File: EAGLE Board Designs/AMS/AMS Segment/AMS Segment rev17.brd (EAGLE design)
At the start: 275.2 x 86 mm, 338 parts, among them J1 CONNECTOR-2_MICROFIT_SMD_RIGH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, J10 CONNECTOR-2_MICROFIT_SMD_RIGH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, J100 CONNECTOR-1_5222_, J101 CONNECTOR-1_5222_, J102 CONNECTOR-1_5222_, J103 CONNECTOR-1_5222_, J104 CONNECTOR-1_5222_, J105 CONNECTOR-1_5222_, J106 CONNECTOR-1_5222_, J107 CONNECTOR-1_5222_, J108 CONNECTOR-1_5222_, J109 CONNECTOR-1_5222_, J110 CONNECTOR-1_5222_, J111 CONNECTOR-1_5222_, J112 CONNECTOR-1_5222_, J113 CONNECTOR-1_5222_, J114 CONNECTOR-1_5222_, J115 CONNECTOR-1_5222_, J116 CONNECTOR-1_5222_, J117 CONNECTOR-1_5222_, J118 CONNECTOR-1_5222_, J119 CONNECTOR-1_5222_, J120 CONNECTOR-1_5222_, J121 CONNECTOR-1_5222_, J2 CONNECTOR-2_MICROFIT_SMD_RIGH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, J3 CONNECTOR-2_MICROFIT_SMD_RIGH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, J4 CONNECTOR-2_MICROFIT_SMD_RIGH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, J5 CONNECTOR-2_MICROFIT_SMD_RIGH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, J6 CONNECTOR-2_MICROFIT_SMD_RIGH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, J7 CONNECTOR-2_MICROFIT_SMD_RIGH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, J8 CONNECTOR-2_MICROFIT_SMD_RIGH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, J9 CONNECTOR-2_MICROFIT_SMD_RIGH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, T1 TRANSFORMER_HM2112ZNLT, U1 LTC6811-2, U2 LTC6811-2, U3 SHT31-ARP-B, U4 SHT31-ARP-B, U5 LT3990-5, U6 LT3990-5

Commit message: Renamed to rev17
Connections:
- net GPIO4L: now also R47.2; no longer R47.1
- net N$90: now also R47.1; no longer R47.2
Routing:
- net VREGL: track 269.5 -> 256.8 mm
- net GPIO4L: track 78.6 -> 74.3 mm
- net N$90: track 23.1 -> 24.3 mm
- net V-L: track 134.3 -> 133.6 mm

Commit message: Working on board changes
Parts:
- moved R48 3.73 mm to (73.2, -3.61)
- moved C29 3.73 mm to (73.2, -6.52)
- moved R45 3.73 mm to (73.2, -9.42)
- moved C31 2.18 mm to (212.2, -8.03)
- moved R46 2.18 mm to (212.2, -10.9)
- moved R50 2.18 mm to (212.2, -5.11)
- moved R10 0.33 mm to (107.3, -71.3)
- moved R11 0.33 mm to (110.8, -71.3)
- moved R8 0.33 mm to (100.4, -71.3)
- moved R9 0.33 mm to (103.9, -71.3)
- turned C30 to 270 degrees
- turned R44 to 270 degrees
- turned R49 to 270 degrees
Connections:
- net CELL10:N$5 renamed CELL10:QG
- net CELL10:N$6 renamed CELL10:QD
- net CELL10:N$7 renamed CELL10:LED
- net CELL11:N$5 renamed CELL11:QG
- net CELL11:N$6 renamed CELL11:QD
- net CELL11:N$7 renamed CELL11:LED
- net CELL12:N$5 renamed CELL12:QG
- net CELL12:N$6 renamed CELL12:QD
- net CELL12:N$7 renamed CELL12:LED
- net CELL13:N$5 renamed CELL13:QG
- net CELL13:N$6 renamed CELL13:QD
- net CELL13:N$7 renamed CELL13:LED
- net CELL14:N$5 renamed CELL14:QG
- net CELL14:N$6 renamed CELL14:QD
- net CELL14:N$7 renamed CELL14:LED
- net CELL15:N$5 renamed CELL15:QG
- net CELL15:N$6 renamed CELL15:QD
- net CELL15:N$7 renamed CELL15:LED
- net CELL16:N$5 renamed CELL16:QG
- net CELL16:N$6 renamed CELL16:QD
- net CELL16:N$7 renamed CELL16:LED
- net CELL17:N$5 renamed CELL17:QG
- net CELL17:N$6 renamed CELL17:QD
- net CELL17:N$7 renamed CELL17:LED
- net CELL18:N$5 renamed CELL18:QG
- net CELL18:N$6 renamed CELL18:QD
- net CELL18:N$7 renamed CELL18:LED
- net CELL19:N$5 renamed CELL19:QG
- net CELL19:N$6 renamed CELL19:QD
- net CELL19:N$7 renamed CELL19:LED
- net CELL1:N$5 renamed CELL1:QG
- net CELL1:N$6 renamed CELL1:QD
- net CELL1:N$7 renamed CELL1:LED
- net CELL20:N$5 renamed CELL20:QG
- net CELL20:N$6 renamed CELL20:QD
- net CELL20:N$7 renamed CELL20:LED
- net CELL21:N$5 renamed CELL21:QG
- net CELL21:N$6 renamed CELL21:QD
- net CELL21:N$7 renamed CELL21:LED
- net CELL2:N$5 renamed CELL2:QG
- net CELL2:N$6 renamed CELL2:QD
- net CELL2:N$7 renamed CELL2:LED
- net CELL3:N$5 renamed CELL3:QG
- net CELL3:N$6 renamed CELL3:QD
- net CELL3:N$7 renamed CELL3:LED
- net CELL4:N$5 renamed CELL4:QG
- net CELL4:N$6 renamed CELL4:QD
- net CELL4:N$7 renamed CELL4:LED
- net CELL5:N$5 renamed CELL5:QG
- net CELL5:N$6 renamed CELL5:QD
- net CELL5:N$7 renamed CELL5:LED
- net CELL6:N$5 renamed CELL6:QG
- net CELL6:N$6 renamed CELL6:QD
- net CELL6:N$7 renamed CELL6:LED
- net CELL7:N$5 renamed CELL7:QG
- net CELL7:N$6 renamed CELL7:QD
- net CELL7:N$7 renamed CELL7:LED
- net CELL8:N$5 renamed CELL8:QG
- net CELL8:N$6 renamed CELL8:QD
- net CELL8:N$7 renamed CELL8:LED
- net CELL9:N$5 renamed CELL9:QG
- net CELL9:N$6 renamed CELL9:QD
- net CELL9:N$7 renamed CELL9:LED
- net GPIO1U: now also C30.2, R44.1; no longer C30.1, R44.2
- net N$71: now also R44.2; no longer R44.1
- net V-U: now also C30.1; no longer C30.2
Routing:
- net N$67: track 61.1 -> 40.1 mm
- net VREGL: track 256.8 -> 245.3 mm
- net V-L: track 133.6 -> 124.4 mm, vias 36 -> 35
- net N$68: track 42.9 -> 35.1 mm
- net S7U: track 79.2 -> 72.0 mm
- net C7U: track 77.3 -> 71.0 mm
- net V-U: track 166.2 -> 162.5 mm
- net GPIO2U: track 82.6 -> 85.6 mm
- net N$76: track 21.1 -> 24.2 mm
- net N$90: track 24.3 -> 21.5 mm
- net N$71: track 19.4 -> 21.1 mm
- net C6U: track 51.7 -> 50.5 mm
- net GPIO3L: track 55.6 -> 56.6 mm
- net N$88: track 21.1 -> 22.1 mm
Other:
- board text added: "HyTech Racing 2022 AMS Segment rev17 Designed by Cody Kaminsky, Noah Bruckner, and Ethan Weinstock Based on rev15 by Arvind Srinivasan"
- board text removed: "HyTech Racing 2022 AMS Segment rev17 Designed by Cody Kaminsky and Noah Bruckner based on rev15 by Arvind Srinivasan"

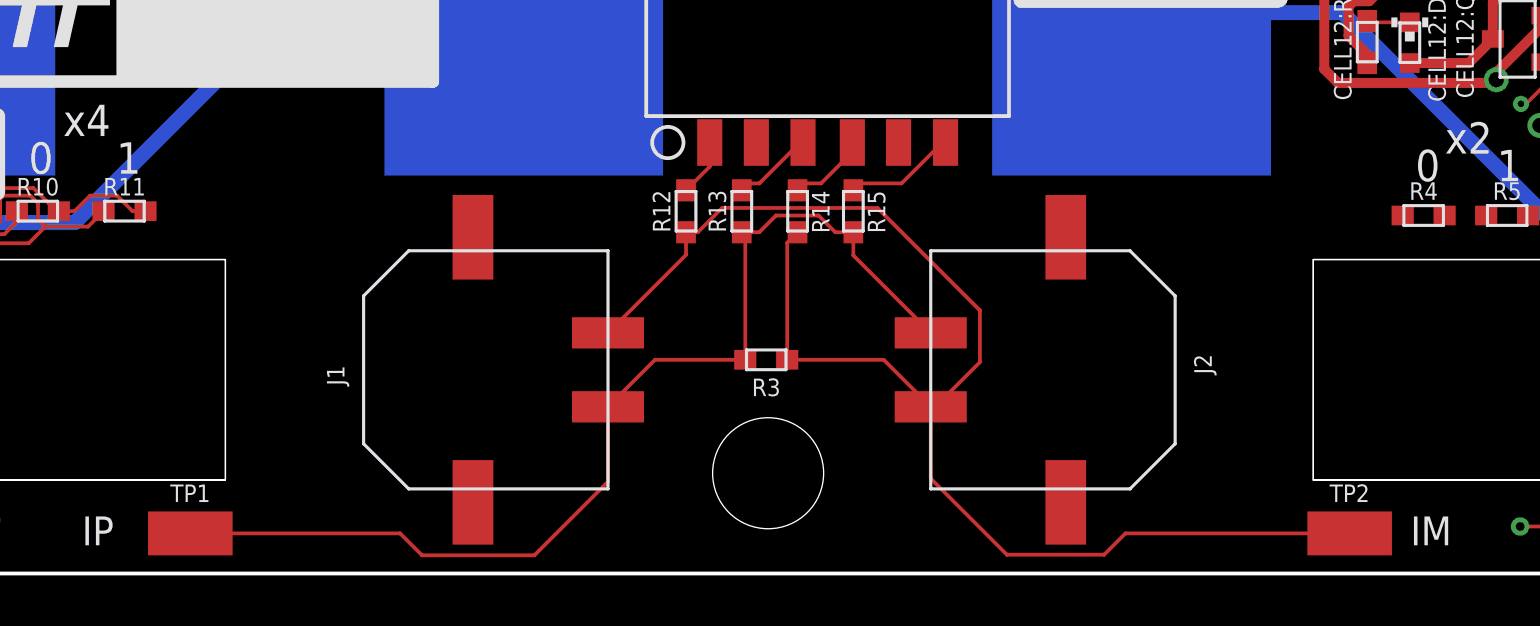
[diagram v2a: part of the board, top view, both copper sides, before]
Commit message: Update AMS Segment rev17.brd
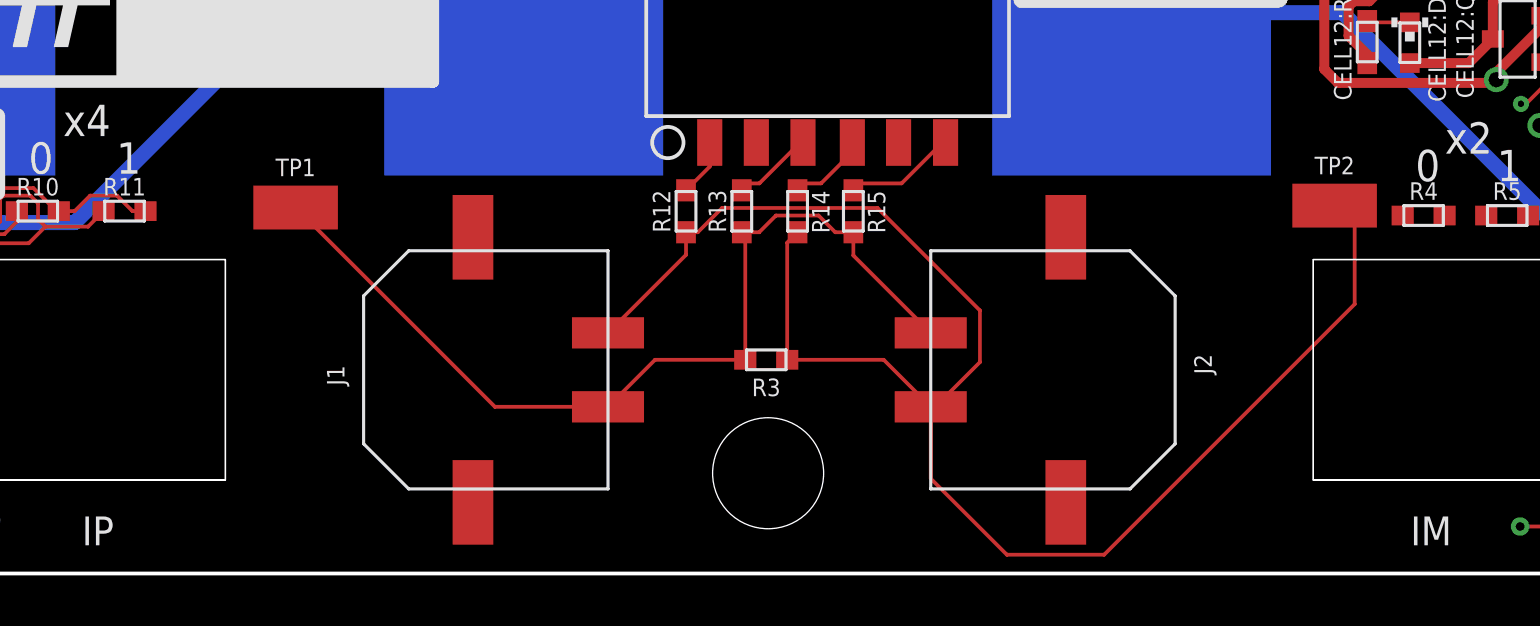
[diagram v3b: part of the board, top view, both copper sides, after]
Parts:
- moved TP1 13.9 mm to (117.8, -71.1)
- moved TP2 13.3 mm to (159.9, -71.1)
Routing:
- net IM: track 57.7 -> 66.4 mm
- net IP: track 43.6 -> 38.0 mm
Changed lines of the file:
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@@
 <attribute name="NAME" x="89.1286" y="-20.0533" size="0.7112" layer="25" font="vector" rot="R270" align="bottom-center"/>
 </element>
-<element name="TP1" library="HyTechDevices" package="MICRO_MINIATURE" value="TEST_POINT" x="113.4872" y="-84.3534" smashed="yes">
-<attribute name="DKPN" value="36-5015CT-ND" x="113.4872" y="-84.3534" size="0.7112" layer="27" font="vector" display="off"/>
-<attribute name="MANUFACTURER" value="Keystone Electronics" x="113.4872" y="-84.3534" size="0.7112" layer="27" font="vector" display="off"/>
-<attribute name="MOPN" value="534-5015" x="113.4872" y="-84.3534" size="0.7112" layer="27" font="vector" display="off"/>
-<attribute name="MPN" value="5015" x="113.4872" y="-84.3534" size="0.7112" layer="27" font="vector" display="off"/>
-<attribute name="NAME" x="113.4872" y="-83.0834" size="0.7112" layer="25" font="vector" align="bottom-center"/>
+<element name="TP1" library="HyTechDevices" package="MICRO_MINIATURE" value="TEST_POINT" x="117.7544" y="-71.1454" smashed="yes">
+<attribute name="DKPN" value="36-5015CT-ND" x="117.7544" y="-71.1454" size="0.7112" layer="27" font="vector" display="off"/>
+<attribute name="MANUFACTURER" value="Keystone Electronics" x="117.7544" y="-71.1454" size="0.7112" layer="27" font="vector" display="off"/>
+<attribute name="MOPN" value="534-5015" x="117.7544" y="-71.1454" size="0.7112" layer="27" font="vector" display="off"/>
+<attribute name="MPN" value="5015" x="117.7544" y="-71.1454" size="0.7112" layer="27" font="vector" display="off"/>
+<attribute name="NAME" x="117.7544" y="-69.8754" size="0.7112" layer="25" font="vector" align="bottom-center"/>
 </element>
-<element name="TP2" library="HyTechDevices" package="MICRO_MINIATURE" value="TEST_POINT" x="160.4772" y="-84.3534" smashed="yes">
-<attribute name="DKPN" value="36-5015CT-ND" x="160.4772" y="-84.3534" size="0.7112" layer="27" font="vector" display="off"/>
-<attribute name="MANUFACTURER" value="Keystone Electronics" x="160.4772" y="-84.3534" size="0.7112" layer="27" font="vector" display="off"/>
-<attribute name="MOPN" value="534-5015" x="160.4772" y="-84.3534" size="0.7112" layer="27" font="vector" display="off"/>
-<attribute name="MPN" value="5015" x="160.4772" y="-84.3534" size="0.7112" layer="27" font="vector" display="off"/>
-<attribute name="NAME" x="160.4772" y="-83.0834" size="0.7112" layer="25" font="vector" align="bottom-center"/>
+<element name="TP2" library="HyTechDevices" package="MICRO_MINIATURE" value="TEST_POINT" x="159.8676" y="-71.0692" smashed="yes">
+<attribute name="DKPN" value="36-5015CT-ND" x="159.8676" y="-71.0692" size="0.7112" layer="27" font="vector" display="off"/>
+<attribute name="MANUFACTURER" value="Keystone Electronics" x="159.8676" y="-71.0692" size="0.7112" layer="27" font="vector" display="off"/>
+<attribute name="MOPN" value="534-5015" x="159.8676" y="-71.0692" size="0.7112" layer="27" font="vector" display="off"/>
+<attribute name="MPN" value="5015" x="159.8676" y="-71.0692" size="0.7112" layer="27" font="vector" display="off"/>
+<attribute name="NAME" x="159.8676" y="-69.7992" size="0.7112" layer="25" font="vector" align="bottom-center"/>
 </element>
 <element name="U3" library="HyTechDevices" package="DFN-8" value="SHT31-ARP-B" x="49.6062" y="-46.3804" smashed="yes">
@@
 <wire x1="143.4973" y1="-79.2226" x2="143.6808875" y2="-79.2226" width="0.1524" layer="1"/>
 <wire x1="145.4912" y1="-77.4122875" x2="143.6808875" y2="-79.2226" width="0.1524" layer="1"/>
-<wire x1="160.4772" y1="-84.3534" x2="151.3897875" y2="-84.3534" width="0.1524" layer="1"/>
-<wire x1="151.3897875" y1="-84.3534" x2="150.5261875" y2="-85.217" width="0.1524" layer="1"/>
+<wire x1="160.6804" y1="-71.3994" x2="160.3502" y2="-71.0692" width="0.1524" layer="1"/>
+<wire x1="159.8676" y1="-71.0692" x2="160.3502" y2="-71.0692" width="0.1524" layer="1"/>
+<wire x1="160.6804" y1="-71.3994" x2="160.6804" y2="-75.0627875" width="0.1524" layer="1"/>
+<wire x1="160.6804" y1="-75.0627875" x2="150.5261875" y2="-85.217" width="0.1524" layer="1"/>
 <wire x1="150.5261875" y1="-85.217" x2="146.5834" y2="-85.217" width="0.1524" layer="1"/>
 <wire x1="146.5834" y1="-85.217" x2="143.4973" y2="-82.1309" width="0.1524" layer="1"/>
@@
 <contactref element="R15" pad="1"/>
 <contactref element="TP1" pad="1"/>
-<wire x1="130.4163" y1="-82.2579" x2="130.4163" y2="-79.2226" width="0.1524" layer="1"/>
 <wire x1="130.4163" y1="-79.2226" x2="132.3213" y2="-77.3176" width="0.1524" layer="1"/>
 <wire x1="132.3213" y1="-77.3176" x2="135.9798" y2="-77.3176" width="0.1524" layer="1"/>
@@
 <wire x1="136.5455125" y1="-72.1478" x2="137.2241125" y2="-71.4692" width="0.1524" layer="1"/>
 <wire x1="138.9500875" y1="-71.4692" x2="139.6286875" y2="-72.1478" width="0.1524" layer="1"/>
-<wire x1="113.4872" y1="-84.3534" x2="121.9904125" y2="-84.3534" width="0.1524" layer="1"/>
-<wire x1="121.9904125" y1="-84.3534" x2="122.8794125" y2="-85.2424" width="0.1524" layer="1"/>
-<wire x1="122.8794125" y1="-85.2424" x2="127.4318" y2="-85.2424" width="0.1524" layer="1"/>
-<wire x1="127.4318" y1="-85.2424" x2="130.4163" y2="-82.2579" width="0.1524" layer="1"/>
+<wire x1="130.4163" y1="-79.2226" x2="125.8316" y2="-79.2226" width="0.1524" layer="1"/>
+<wire x1="125.8316" y1="-79.2226" x2="117.7544" y2="-71.1454" width="0.1524" layer="1"/>
 </signal>
 <signal name="SENSE12" class="4">

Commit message: Only fix left is address resistors
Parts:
- moved D2 14.9 mm to (118.2, -84.1)
- moved R2 14.9 mm to (115.2, -84.1)
- moved D1 14.0 mm to (155.6, -84.1)
- moved R1 14.0 mm to (158.8, -84.1)
- moved TP2 3.79 mm to (156.1, -71.1)
- moved U$21 2.54 mm to (270.3, -5.71)
- moved C30 0.69 mm to (36.4, -8.13)
- moved R44 0.69 mm to (36.4, -11.0)
- moved R49 0.69 mm to (36.4, -5.21)
- moved C32 0.08 mm to (248.2, -8.05)
- moved R51 0.08 mm to (248.2, -5.13)
- moved TP1 0.08 mm to (117.8, -71.1)
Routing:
- net N$54: track 49.7 -> 31.7 mm
- net VREGL: track 245.3 -> 260.4 mm
- net IM: track 66.4 -> 52.1 mm
- net V-U: track 162.5 -> 151.5 mm
- net IPU: track 83.6 -> 72.9 mm
- net IMU: track 79.8 -> 69.2 mm
- net N$25: track 45.7 -> 36.2 mm
- net SENSE5: track 87.0 -> 78.1 mm, vias 2 -> 0
- net V-L: track 124.4 -> 126.7 mm, vias 35 -> 34
- net N$90: track 21.5 -> 23.7 mm
- net GPIO3L: track 56.6 -> 55.7 mm
- net SENSE13: track 88.1 -> 87.3 mm, vias 2 -> 0
- net VREGU: vias 5 -> 7

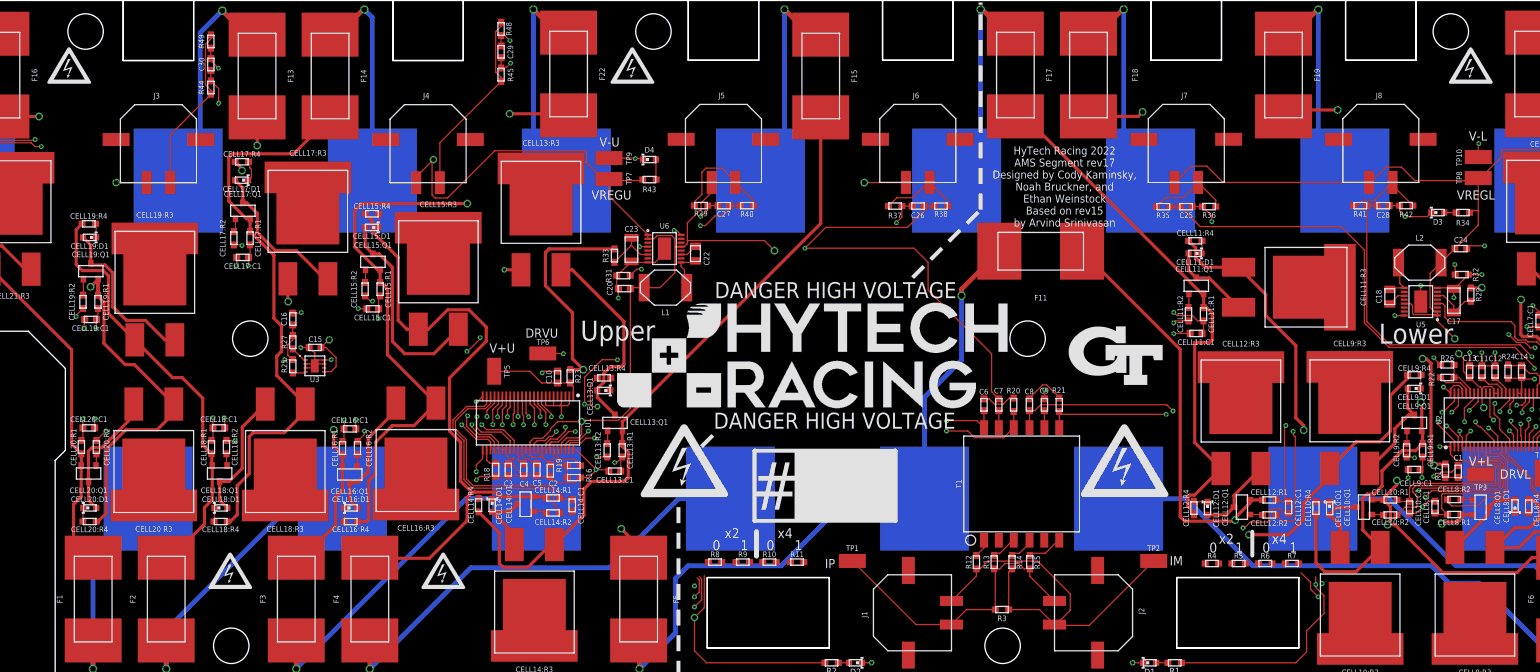
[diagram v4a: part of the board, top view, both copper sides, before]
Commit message: fixed some silkscreen
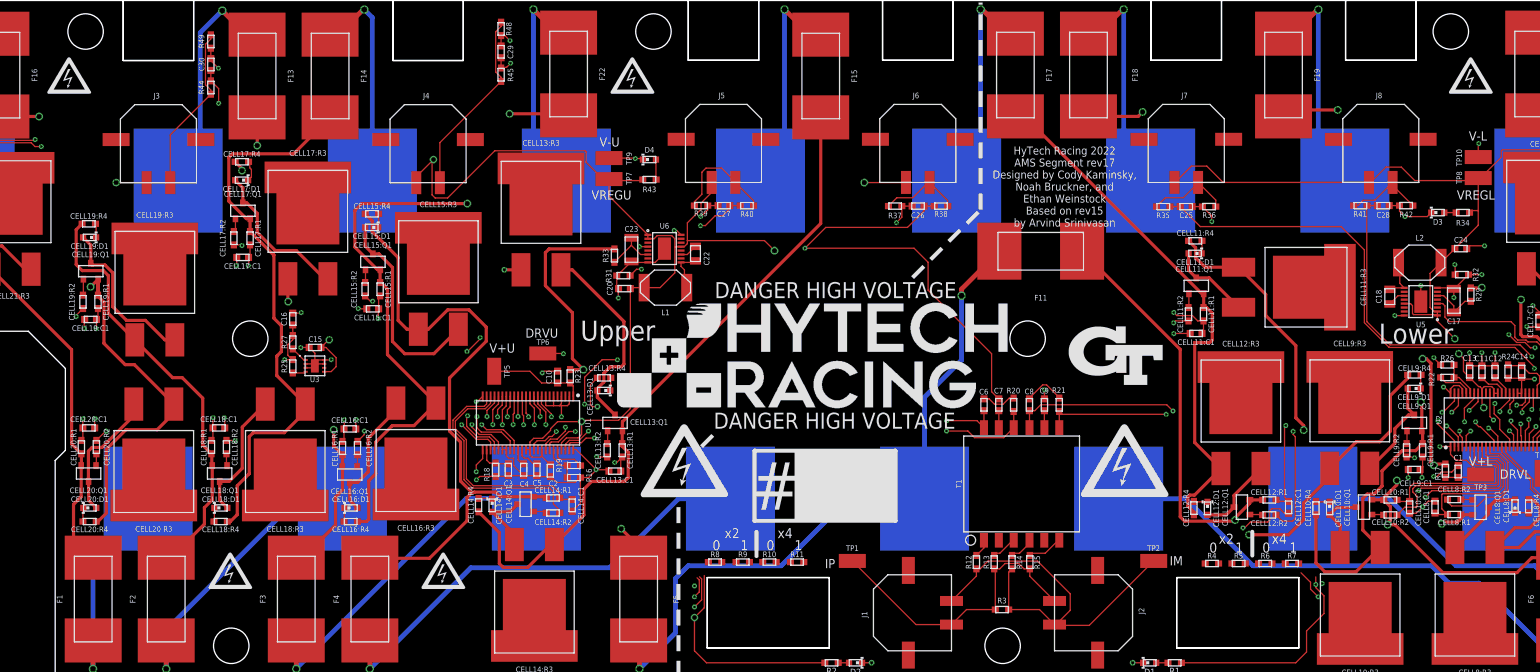
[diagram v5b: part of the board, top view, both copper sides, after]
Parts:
- moved U$18 1.27 mm to (18.4, -9.53)
- moved U$19 1.27 mm to (89.9, -9.53)
- moved U$20 1.27 mm to (196.3, -9.53)
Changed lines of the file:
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@@
 <text x="157.226" y="-46.609" size="3.81" layer="22" font="vector" rot="MR0">Lower</text>
 <text x="106.68" y="-46.609" size="3.81" layer="22" font="vector" rot="MR0">Upper</text>
-<wire x1="105.664" y1="-70.5358" x2="105.664" y2="-67.437" width="0.635" layer="21"/>
+<wire x1="105.664" y1="-70.5358" x2="105.664" y2="-67.437" width="0.508" layer="21"/>
 <wire x1="168.6052" y1="-70.4596" x2="168.6052" y2="-67.437" width="0.508" layer="21"/>
 <text x="100.076" y="-69.7738" size="1.27" layer="21" font="vector">0</text>
@@
 <attribute name="MOPN" value="" x="136.8298" y="-77.3176" size="0.7112" layer="27" font="vector" rot="R180" display="off"/>
 <attribute name="MPN" value="" x="136.8298" y="-77.3176" size="0.7112" layer="27" font="vector" rot="R180" display="off"/>
-<attribute name="NAME" x="136.8298" y="-78.0796" size="0.7112" layer="25" font="vector" rot="R180" align="bottom-center"/>
+<attribute name="NAME" x="136.8298" y="-76.5302" size="0.7112" layer="25" font="vector" align="bottom-center"/>
 <attribute name="POWER" value="" x="136.8298" y="-77.3176" size="0.7112" layer="27" font="vector" rot="R180" display="off"/>
 <attribute name="RESISTANCE" value="DNP" x="136.8298" y="-77.3176" size="0.7112" layer="27" font="vector" rot="R180" display="off"/>
@@
 <element name="U$4" library="HyTechAesthetics" package="HV_0.50&quot;" value="" x="38.862" y="-72.39" smashed="yes"/>
 <element name="U$5" library="HyTechAesthetics" package="HV_0.50&quot;" value="" x="65.913" y="-72.39" smashed="yes"/>
-<element name="U$18" library="HyTechAesthetics" package="HV_0.50&quot;" value="" x="18.415" y="-8.255" smashed="yes"/>
-<element name="U$19" library="HyTechAesthetics" package="HV_0.50&quot;" value="" x="89.916" y="-8.255" smashed="yes"/>
-<element name="U$20" library="HyTechAesthetics" package="HV_0.50&quot;" value="" x="196.342" y="-8.255" smashed="yes"/>
+<element name="U$18" library="HyTechAesthetics" package="HV_0.50&quot;" value="" x="18.415" y="-9.525" smashed="yes"/>
+<element name="U$19" library="HyTechAesthetics" package="HV_0.50&quot;" value="" x="89.916" y="-9.525" smashed="yes"/>
+<element name="U$20" library="HyTechAesthetics" package="HV_0.50&quot;" value="" x="196.342" y="-9.525" smashed="yes"/>
 <element name="U$21" library="HyTechAesthetics" package="HV_0.50&quot;" value="" x="270.256" y="-5.715" smashed="yes"/>
 <element name="U$13" library="HyTechAesthetics" package="HV_0.50&quot;" value="" x="232.791" y="-44.45" smashed="yes"/>
